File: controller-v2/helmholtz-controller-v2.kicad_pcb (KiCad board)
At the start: 2 copper layers, 72.7 x 72.1 mm, 54 parts, among them J1 Screw_Terminal_01x02, J2 Screw_Terminal_01x02, J3 Screw_Terminal_01x02, J4 Screw_Terminal_01x02, J5 Conn_01x04, U1 BDS63150AFM, U2 BDS63150AFM, U3 INA226, U4 INA226, U5 BDS63150AFM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

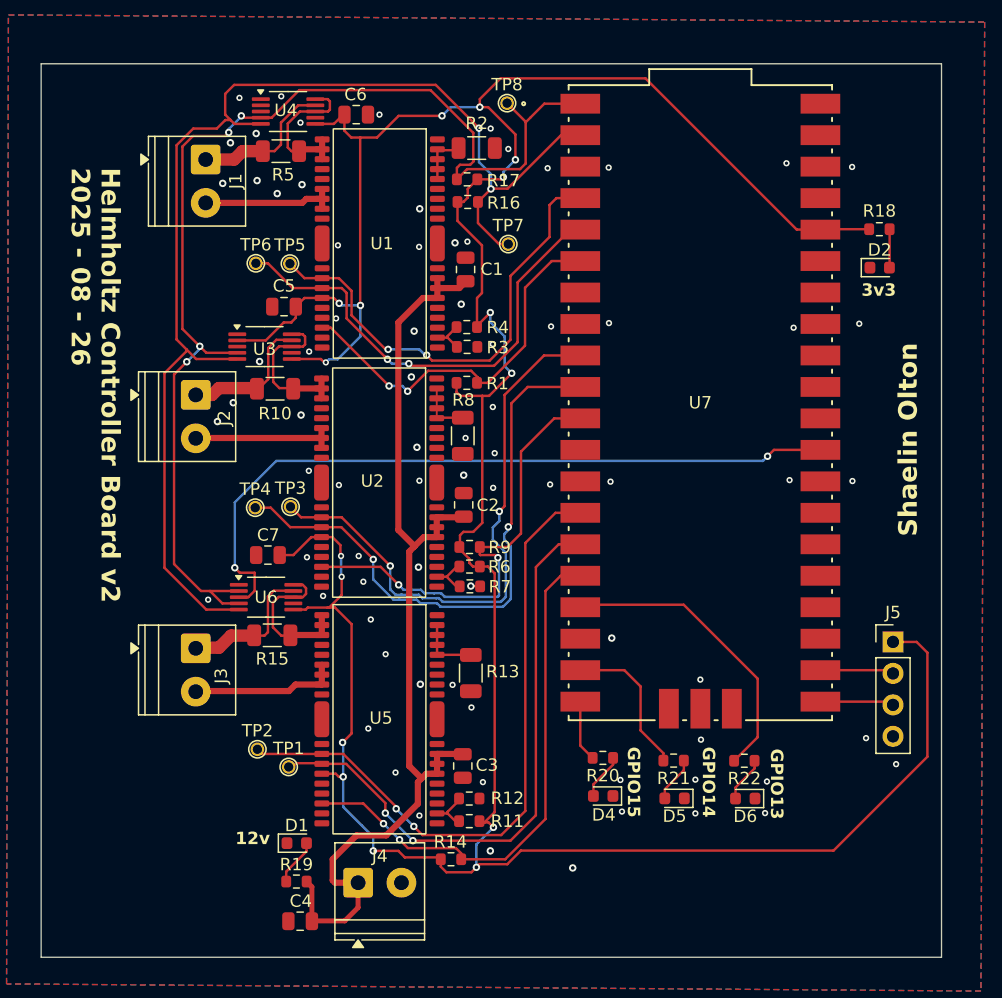
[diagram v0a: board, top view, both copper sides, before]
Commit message: Added mounting holes to schematic & connected alert pins on PCB.
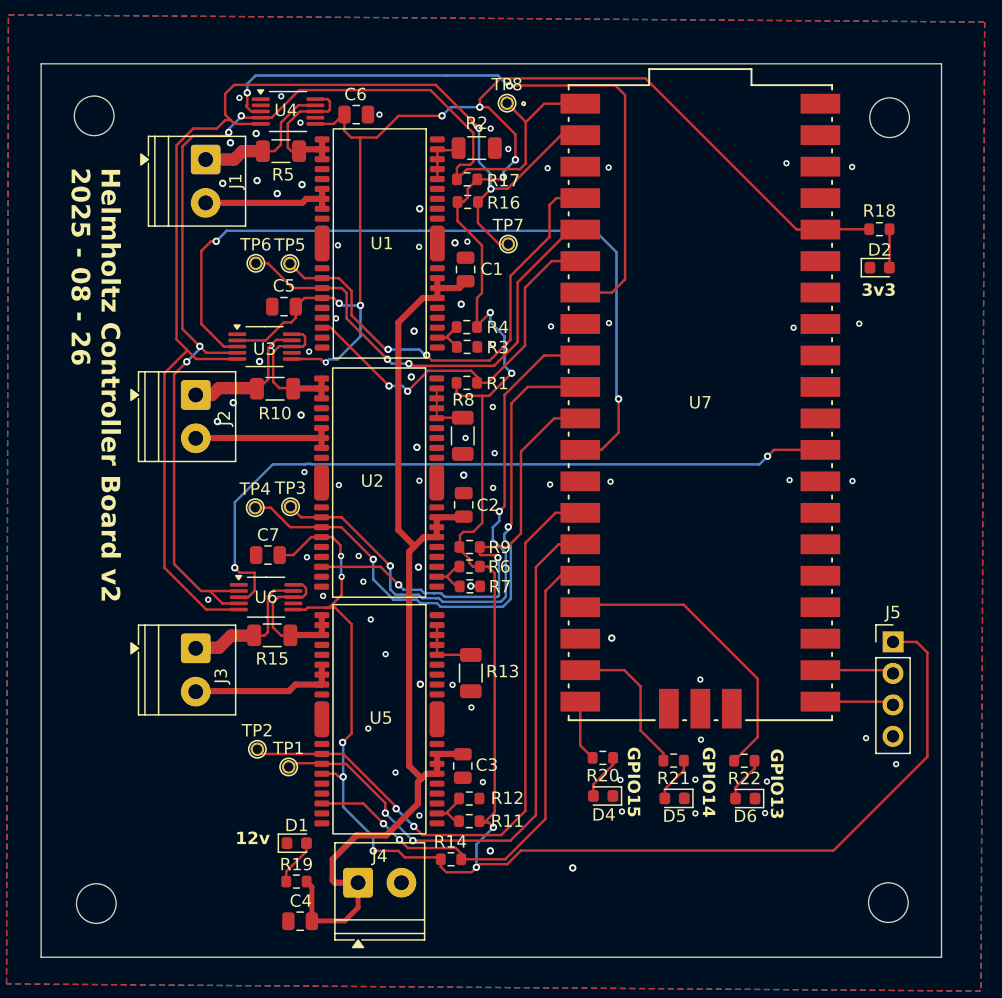
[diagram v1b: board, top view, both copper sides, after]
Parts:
- added H1: MountingHole, MountingHole:MountingHole_3.2mm_M3, F.Cu at (65.2, 51.2)
- added H2: MountingHole, MountingHole:MountingHole_3.2mm_M3, F.Cu at (65.3, 114.8)
- added H3: MountingHole, MountingHole:MountingHole_3.2mm_M3, F.Cu at (129.3, 51.4)
- added H4: MountingHole, MountingHole:MountingHole_3.2mm_M3, F.Cu at (129.2, 114.7)
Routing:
- net Net-(U3-~{Alert}): track 0.00 -> 62.8 mm, vias 0 -> 2
- net Net-(U4-~{Alert}): track 0.00 -> 53.6 mm, vias 0 -> 2

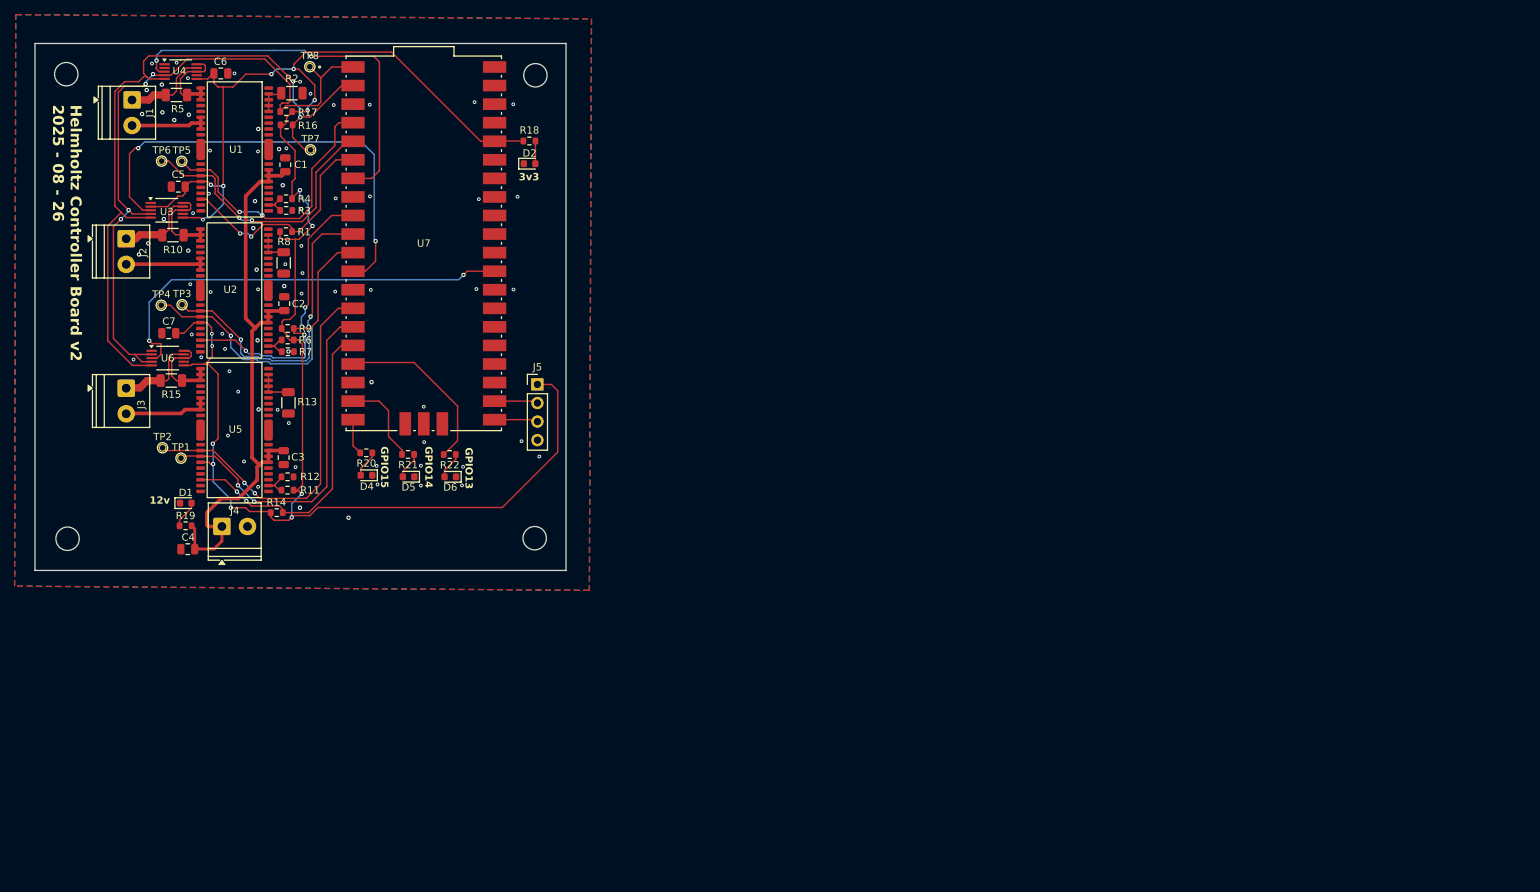
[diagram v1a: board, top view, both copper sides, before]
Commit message: fix schematic and layout sync issues. Begin reworking layout to reduce side flipping.
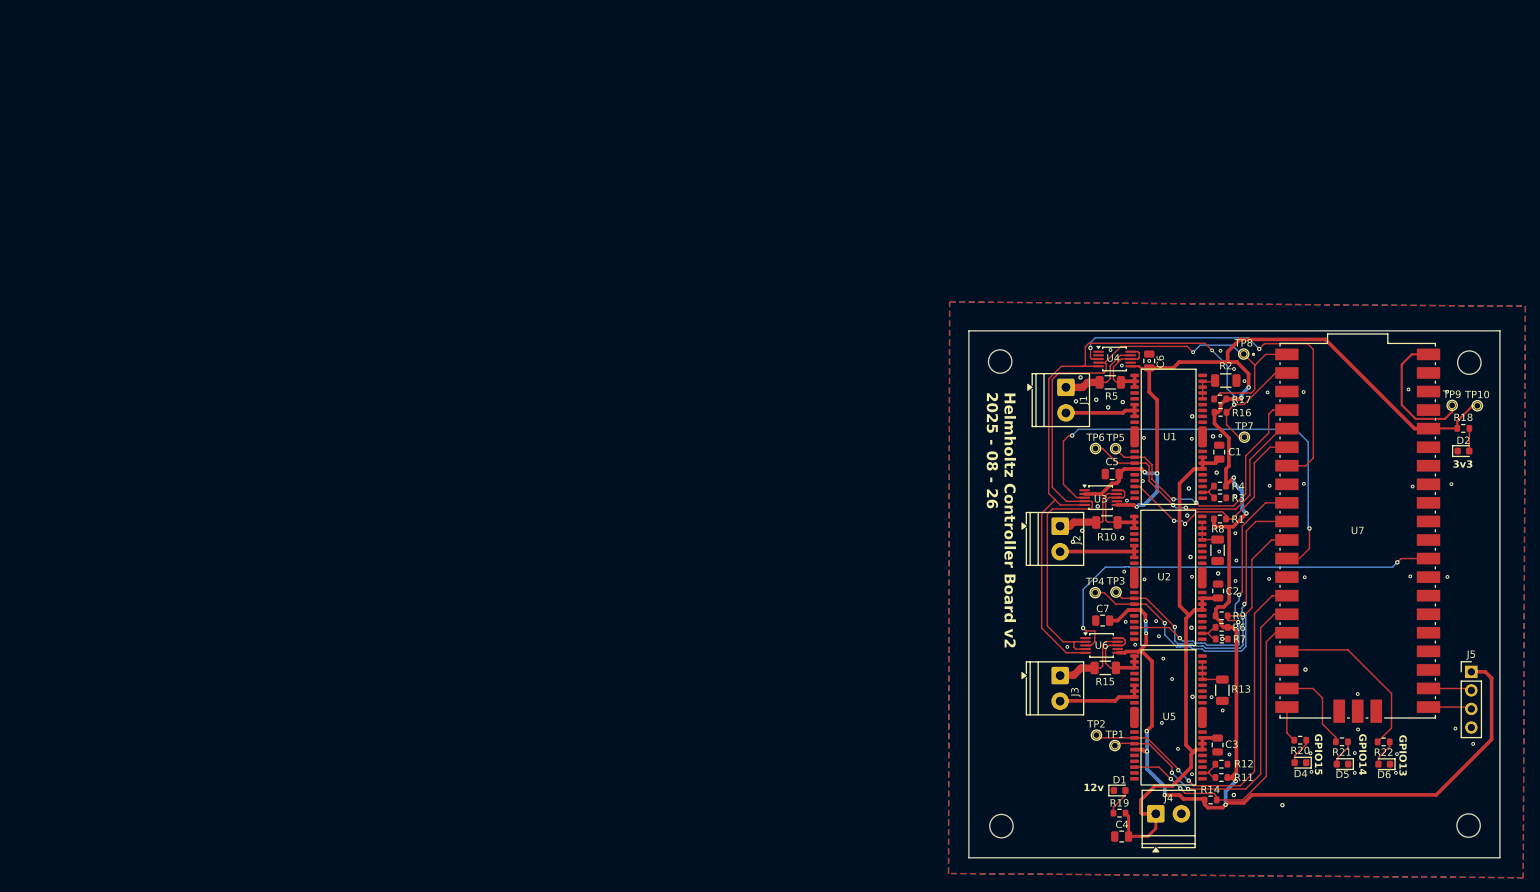
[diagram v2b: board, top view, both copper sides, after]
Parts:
- added TP10: Test-Point, oresat-misc:TestPoint-0.75mm-th, F.Cu at (258.2, 96.6)
- added TP9: Test-Point, oresat-misc:TestPoint-0.75mm-th, F.Cu at (254.8, 96.5)
- D1, D2: value LED -> GRN
- D4, D5, D6: value LED -> AMBER
- R18, R20, R21, R22: value 660 -> 1k
- R19: value 2.4k -> 4.7k
- moved C1 133.7 mm to (222.9, 102.9)
- moved C2 133.7 mm to (222.8, 121.9)
- moved C5 133.7 mm to (208.3, 105.9)
- moved D1 133.7 mm to (209.3, 149.2)
- moved D2 133.7 mm to (256.4, 102.8)
- moved H4 133.7 mm to (257.1, 154.0)
- moved J2 133.7 mm to (201.2, 113.0)
- moved J3 133.7 mm to (201.2, 133.5)
- moved J5 133.7 mm to (257.4, 133.0)
- moved R1 133.7 mm to (223.0, 112.1)
- moved R10 133.7 mm to (207.6, 112.5)
- moved R17 133.7 mm to (223.1, 95.7)
- moved R19 133.7 mm to (209.3, 152.3)
- moved R22 133.7 mm to (245.4, 142.6)
- moved R3 133.7 mm to (223.1, 109.2)
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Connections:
- net Net-(U1-IN1) renamed /X_IN1
- net Net-(U1-IN2) renamed /X_IN2
- net Net-(U1-~{FAILA}) renamed /X_FAIL
- net Net-(U4-~{Alert}) renamed /X_INA_ALERT
- U7 pad 23: unconnected-(U7-GND-Pad23) -> GND
- U7 pad 40: +5.0V -> Net-(U7-VBUS)
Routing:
- net Net-(U7-VBUS): track 0.00 -> 18.7 mm
- net +3.3V: track 267.9 -> 272.1 mm, vias 16 -> 14
- net SDA: track 95.7 -> 99.7 mm, vias 4 -> 1
- net /X_INA_ALERT: track 53.6 -> 54.2 mm
- net Net-(J2-Pin_1): track 11.7 -> 12.2 mm
- net GND: vias 77 -> 76

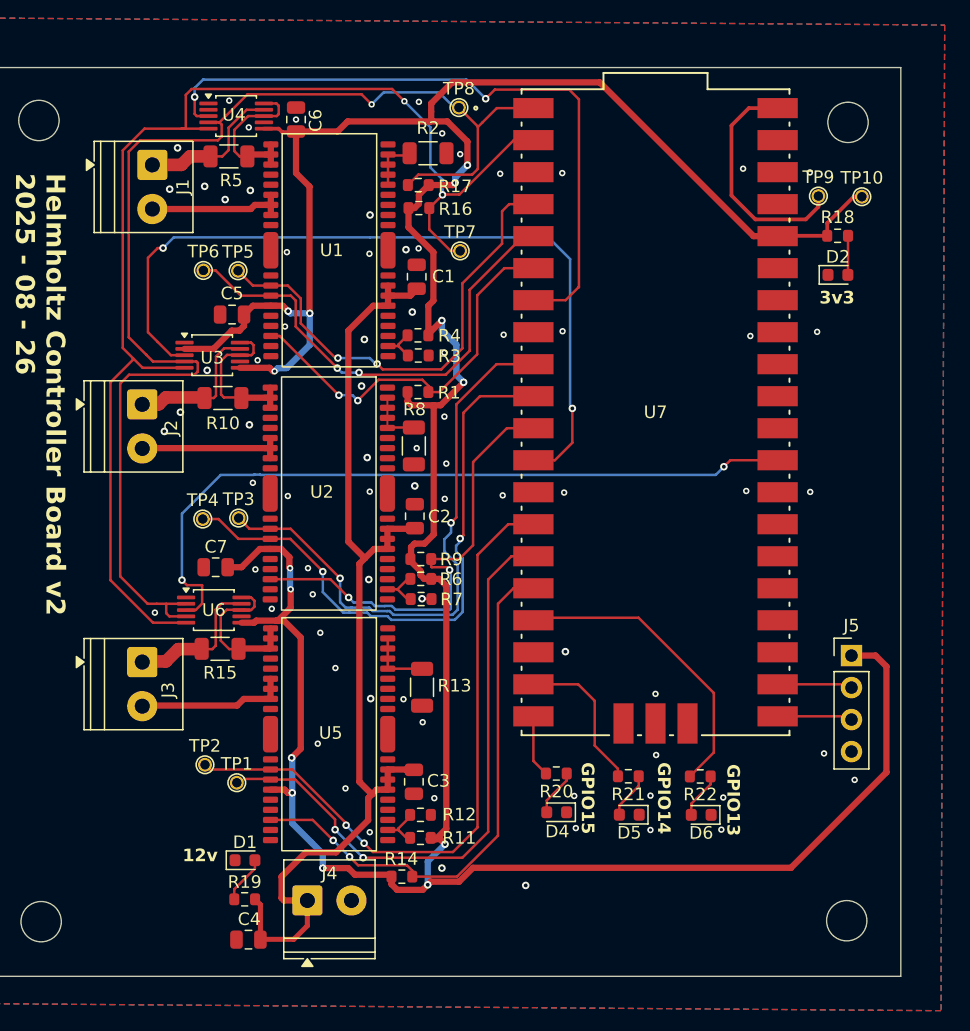
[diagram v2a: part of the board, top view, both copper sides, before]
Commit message: Rerouted 3.3v & 12v, added zones
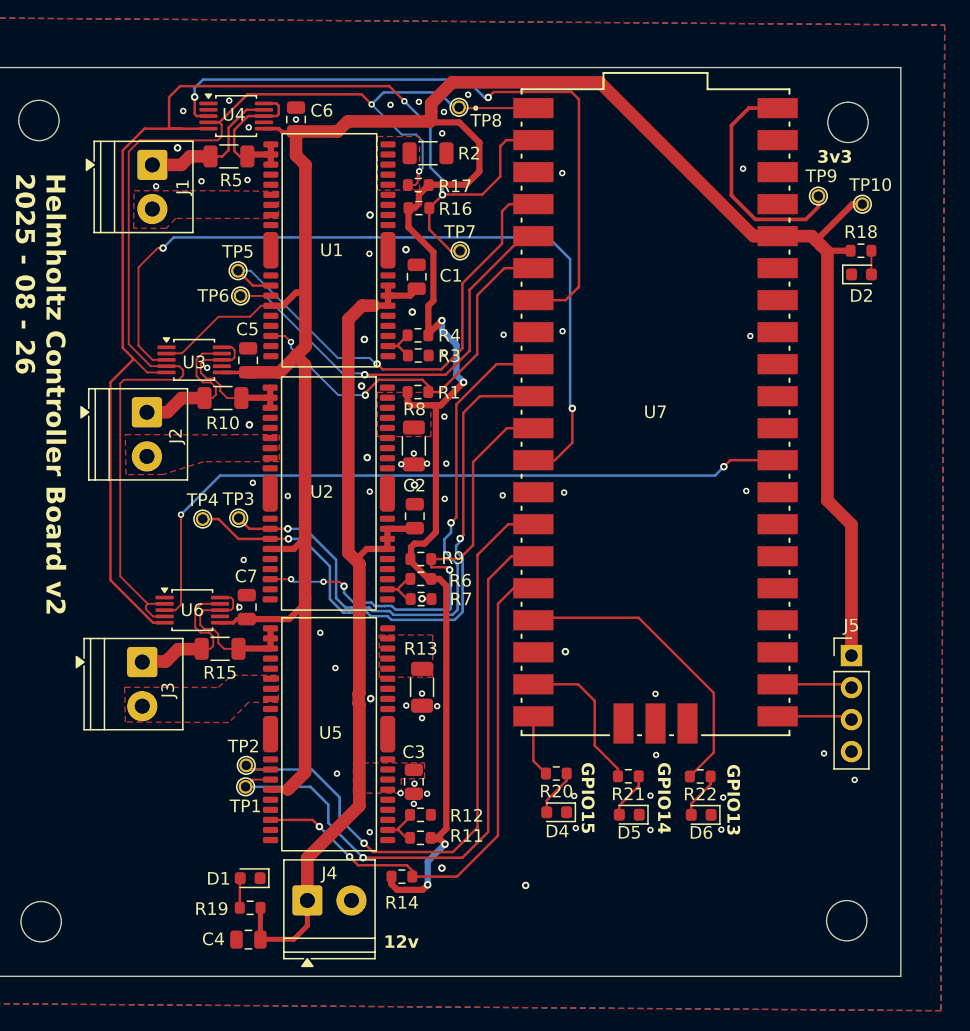
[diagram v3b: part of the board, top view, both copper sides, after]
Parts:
- moved C7 4.01 mm to (209.4, 129.1), turned to -90 degrees
- moved C5 3.85 mm to (209.6, 109.6), turned to -90 degrees
- moved TP6 3.58 mm to (208.9, 104.5)
- moved TP2 3.28 mm to (209.4, 141.7)
- moved R18 2.20 mm to (258.2, 100.9)
- moved D2 1.87 mm to (258.2, 102.7)
- moved U6 1.71 mm to (205.1, 129.4)
- moved D1 1.48 mm to (209.7, 150.7), turned to 180 degrees
- moved U3 1.48 mm to (205.3, 109.5)
- moved R19 0.80 mm to (209.7, 153.0)
- moved TP1 0.77 mm to (209.3, 143.4)
- moved J2 0.73 mm to (201.5, 113.7)
- moved TP10 0.60 mm to (258.3, 97.2)
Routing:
- net Net-(J2-Pin_2): track 11.5 -> 0.25 mm
- net Net-(J3-Pin_2): track 11.2 -> 0.00 mm
- net Net-(J1-Pin_2): track 11.1 -> 0.00 mm
- net +12V: track 81.4 -> 71.3 mm
- net +3.3V: track 272.1 -> 263.5 mm, vias 14 -> 4
- net SDA: track 99.7 -> 94.1 mm, vias 1 -> 2
- net Net-(U5-RNFS): track 4.29 -> 0.00 mm
- net Net-(U1-RNFS): track 4.62 -> 0.35 mm
- net Net-(U2-RNFS): track 4.24 -> 0.18 mm
- net /X_IN2: track 38.2 -> 35.6 mm, vias 2 -> 1
- net /X_IN1: track 37.8 -> 39.7 mm, vias 2 -> 1
- net Net-(U5-IN2): track 48.4 -> 49.9 mm, vias 2 -> 1
- net Net-(D1-A): track 3.40 -> 2.01 mm
- net Net-(U6-~{Alert}): track 59.0 -> 57.8 mm
- net Net-(D2-A): track 3.11 -> 1.88 mm
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- added copper zone on F.Cu, net +12V
- added copper zone on F.Cu, net Net-(J1-Pin_2)
- added copper zone on F.Cu, net Net-(J2-Pin_2)
- added copper zone on F.Cu, net Net-(J3-Pin_2)
- added copper zone on F.Cu, net Net-(U1-RNFS)
- added copper zone on F.Cu, net Net-(U2-RNFS)
- added copper zone on F.Cu, net Net-(U5-RNFS)

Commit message: Added zones to shunt resistors
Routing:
- net Net-(U6-Vbus): track 13.5 -> 9.78 mm
- net Net-(U3-Vbus): track 13.2 -> 9.61 mm
- net Net-(U4-Vbus): track 12.6 -> 9.14 mm
- net GND: vias 70 -> 71
- added copper zone on F.Cu, net Net-(U3-Vbus)
- added copper zone on F.Cu, net Net-(U4-Vbus)
- added copper zone on F.Cu, net Net-(U6-Vbus)
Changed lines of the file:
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@@
 	)
 	(segment
-		(start 211.3 112.525)
-		(end 211.3 111.725)
-		(width 0.5)
-		(layer "F.Cu")
-		(net 1)
-	)
-	(segment
 		(start 208.48 109.32)
 		(end 208.28 109.52)
@@
 	)
 	(segment
-		(start 211.3 112.525)
-		(end 211.3 113.325)
-		(width 0.5)
-		(layer "F.Cu")
-		(net 1)
-	)
-	(segment
 		(start 207.89 112.55)
 		(end 207.34 112)
@@
 	)
 	(segment
-		(start 211.3 112.525)
-		(end 209.31875 112.525)
-		(width 0.5)
-		(layer "F.Cu")
-		(net 1)
-	)
-	(segment
 		(start 209.0125 112.55)
 		(end 207.89 112.55)
@@
 	)
 	(via
+		(at 203.05 108.05)
+		(size 0.508)
+		(drill 0.254)
+		(layers "F.Cu" "B.Cu")
+		(free yes)
+		(net 7)
+	)
+	(via
 		(at 241.475 144.1)
 		(size 0.508)
@@
 	)
 	(segment
-		(start 209.6875 93.225)
-		(end 211.35 93.225)
-		(width 0.5)
-		(layer "F.Cu")
-		(net 9)
-	)
-	(segment
 		(start 211.975 90.025)
 		(end 211.825 90.175)
@@
 	)
 	(segment
-		(start 211.35 93.225)
-		(end 211.35 94.025)
-		(width 0.5)
-		(layer "F.Cu")
-		(net 9)
-	)
-	(segment
 		(start 211.8 89.175)
 		(end 211.975 89.35)
@@
 	)
 	(segment
-		(start 211.2 93.375)
-		(end 211.35 93.225)
-		(width 0.2)
-		(layer "F.Cu")
-		(net 9)
-	)
-	(segment
 		(start 209.5125 93.4)
 		(end 209.6875 93.225)
@@
 	)
 	(segment
-		(start 211.35 93.225)
-		(end 211.35 92.425)
-		(width 0.5)
-		(layer "F.Cu")
-		(net 9)
-	)
-	(segment
 		(start 208.875 93.375)
 		(end 208.45 92.95)
@@
 	)
 	(segment
-		(start 209.0875 132.425)
-		(end 211.225 132.425)
-		(width 0.5)
-		(layer "F.Cu")
-		(net 11)
-	)
-	(segment
 		(start 206.0642 130.8642)
 		(end 205.75 130.55)
@@
 	)
 	(segment
-		(start 211.325 132.425)
-		(end 211.325 130.825)
-		(width 0.5)
-		(layer "F.Cu")
-		(net 11)
-	)
-	(segment
 		(start 207.18 131.98)
 		(end 207.18 131.27)
@@
 	)
 	(zone
+		(net 1)
+		(net_name "Net-(U3-Vbus)")
+		(layer "F.Cu")
+		(hatch edge 0.5)
+		(priority 3)
+		(connect_pads yes
+			(clearance 0.2)
+		)
+		(min_thickness 0.1524)
+		(filled_areas_thickness no)
+		(fill yes
+			(thermal_gap 0.5)
+			(thermal_bridge_width 0.5)
+			(smoothing fillet)
+			(radius 0.2)
+		)
+		(polygon
+			(pts
+				(xy 212.050202 111.099916) (xy 212.049259 113.899916) (xy 208.097474 113.899916) (xy 208.1484 111.099916)
+			)
+		)
+	)
+	(zone
+		(net 11)
+		(net_name "Net-(U6-Vbus)")
+		(layer "F.Cu")
+		(hatch edge 0.5)
+		(priority 3)
+		(connect_pads yes
+			(clearance 0.2)
+		)
+		(min_thickness 0.1524)
+		(filled_areas_thickness no)
+		(fill yes
+			(thermal_gap 0.5)
+			(thermal_bridge_width 0.5)
+			(smoothing fillet)
+			(radius 0.2)
+		)
+		(polygon
+			(pts
+				(xy 212.050909 130.55) (xy 212.049966 133.35) (xy 208.098181 133.35) (xy 208.149107 130.55)
+			)
+		)
+	)
+	(zone
 		(net 22)
 		(net_name "Net-(U5-RNFS)")
@@
 			)
 		)
+	)
+	(zone
+		(net 9)
+		(net_name "Net-(U4-Vbus)")
+		(layer "F.Cu")
+		(hatch edge 0.5)
+		(priority 3)
+		(connect_pads yes
+			(clearance 0.2)
+		)
+		(min_thickness 0.1524)
+		(filled_areas_thickness no)
+		(fill yes
+			(thermal_gap 0.5)
+			(thermal_bridge_width 0.5)
+			(smoothing fillet)
+			(radius 0.2)
+		)
+		(polygon
+			(pts
+				(xy 212.300202 91.849916) (xy 212.299259 94.649916) (xy 208.697474 94.649916) (xy 208.7484 91.849916)
+			)
+		)
